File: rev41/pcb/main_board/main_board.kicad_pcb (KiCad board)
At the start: 2 copper layers, 116.1 x 100.8 mm, 85 parts, among them J1 Conn_02x10_Odd_Even, J2 Conn_02x10_Odd_Even, SW1 SW_Push_45deg, SW10 SW_Push_45deg, SW11 SW_Push_45deg, SW12 SW_Push_45deg, SW13 SW_Push_45deg, SW14 SW_Push_45deg, SW15 SW_Push_45deg, SW16 SW_Push_45deg, SW17 SW_Push_45deg, SW18 SW_Push_45deg, SW19 SW_Push_45deg, SW2 SW_Push_45deg, SW20 SW_Push_45deg, SW21 SW_Push_45deg, SW22 SW_Push_45deg, SW23 SW_Push_45deg, SW24 SW_Push_45deg, SW25 SW_Push_45deg, SW26 SW_Push_45deg, SW27 SW_Push_45deg, SW28 SW_Push_45deg, SW29 SW_Push_45deg, SW3 SW_Push_45deg, SW4 SW_Push_45deg, SW5 SW_Push_45deg, SW6 SW_Push_45deg, SW7 SW_Push_45deg, SW8 SW_Push_45deg, SW9 SW_Push_45deg

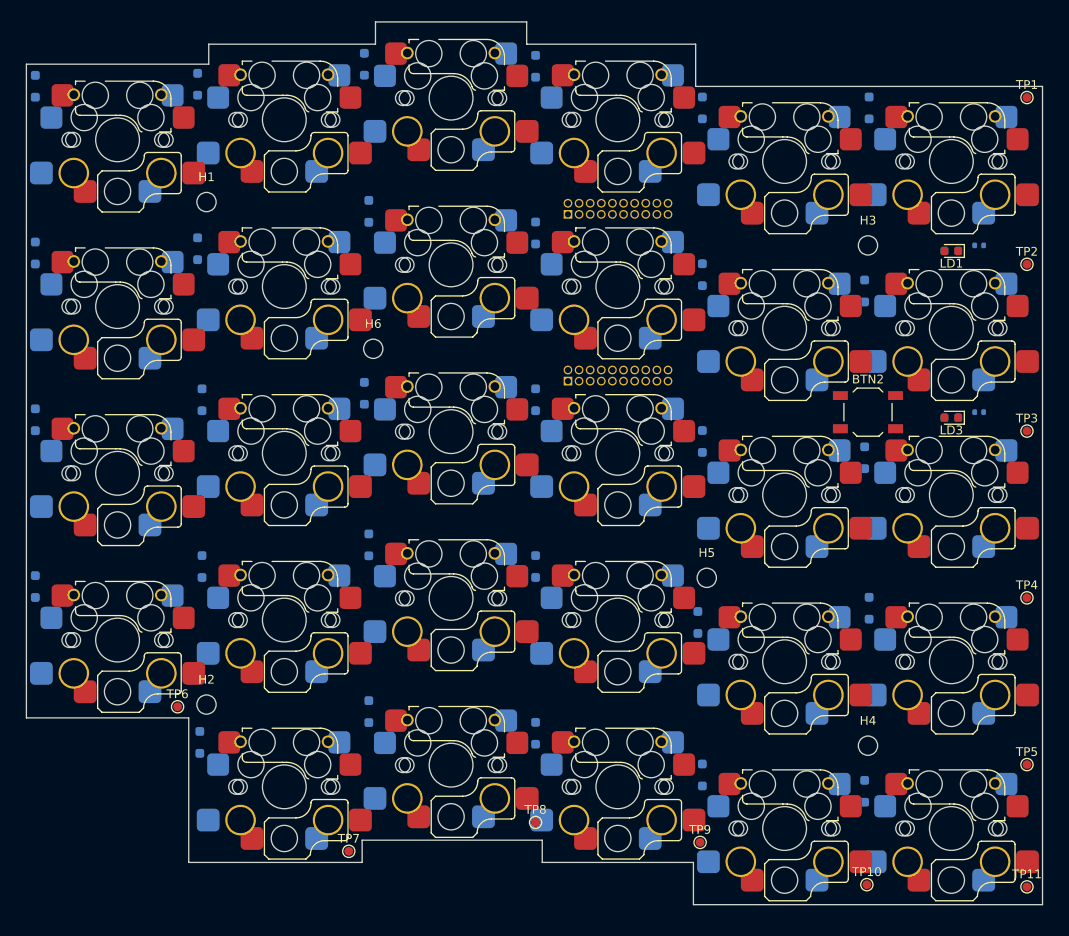
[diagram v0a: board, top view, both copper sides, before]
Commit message: feat: basic routed
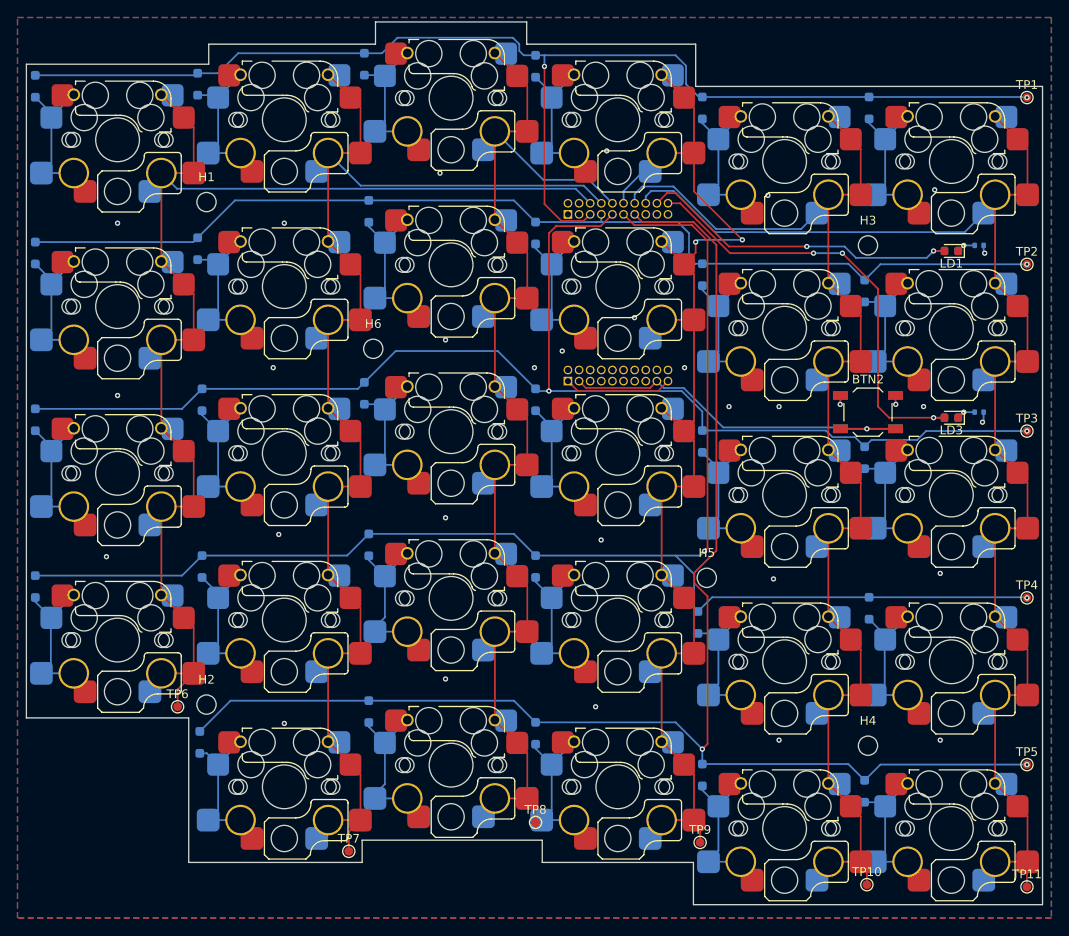
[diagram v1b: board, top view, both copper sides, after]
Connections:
- J1 pad 12: COL_5 -> COL_3
- J1 pad 16: COL_3 -> COL_5
- J1 pad 6: COL_1 -> COL_0
- J1 pad 8: COL_0 -> COL_1
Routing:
- net ROW_3: track 0.00 -> 171.9 mm, vias 0 -> 2
- net ROW_4: track 0.00 -> 171.7 mm, vias 0 -> 2
- net COL_5: track 0.00 -> 156.7 mm
- net COL_1: track 0.00 -> 149.0 mm
- net ROW_2: track 0.00 -> 148.7 mm, vias 0 -> 2
- net ROW_0: track 0.00 -> 142.9 mm, vias 0 -> 2
- net COL_0: track 0.00 -> 142.0 mm
- net COL_4: track 0.00 -> 139.2 mm
- net COL_3: track 0.00 -> 135.4 mm, vias 0 -> 2
- net COL_2: track 0.00 -> 131.3 mm
- net ROW_1: track 0.00 -> 122.9 mm, vias 0 -> 1
- net LED_2: track 0.00 -> 50.9 mm, vias 0 -> 3
- net RESET: track 0.00 -> 45.4 mm, vias 0 -> 1
- net LED_1: track 0.00 -> 38.0 mm, vias 0 -> 2
- net Net-(D17-A): track 0.00 -> 17.3 mm
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- added copper zone on B.Cu, net GND
- added copper zone on F.Cu, net GND

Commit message: feat: add thumb cluster
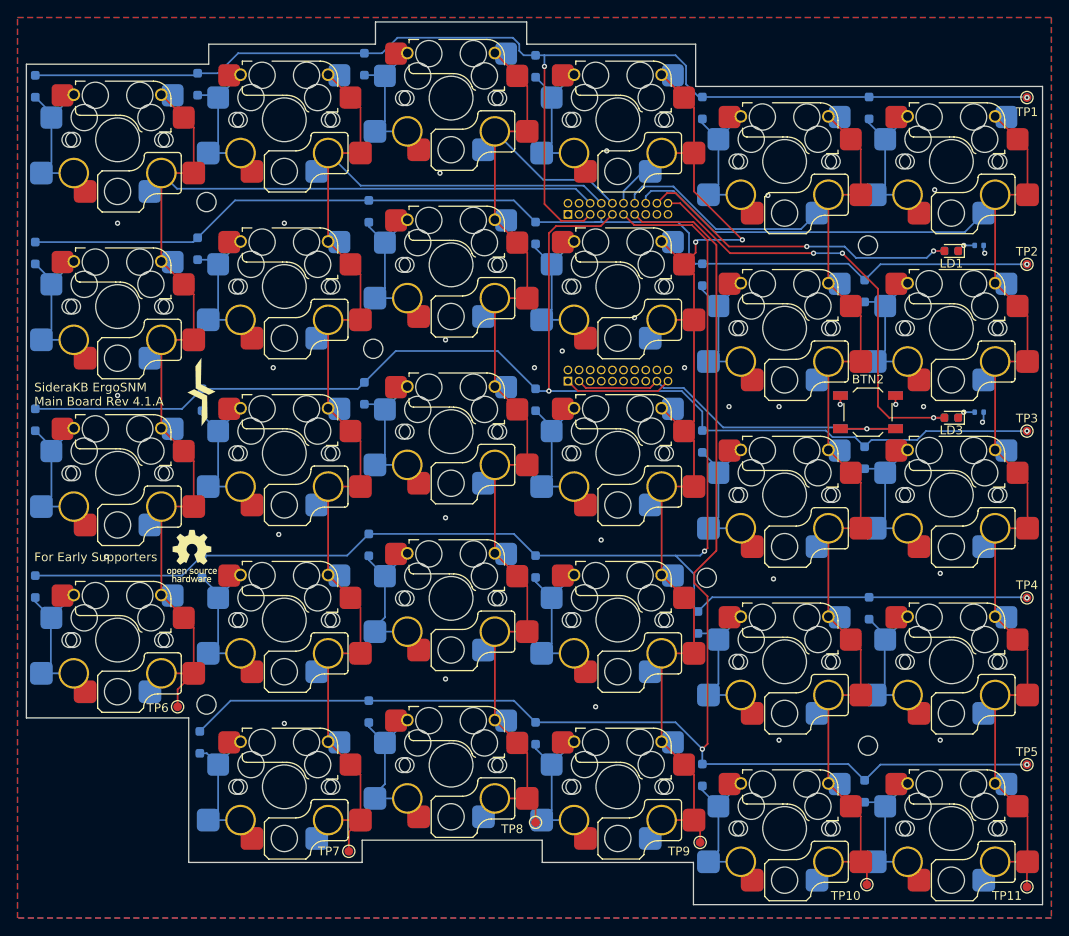
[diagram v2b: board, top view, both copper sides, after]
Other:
- board text added: "For Early Supporters"
- board text added: "SideraKB ErgoSNM Main Board Rev ${REVISION}"
